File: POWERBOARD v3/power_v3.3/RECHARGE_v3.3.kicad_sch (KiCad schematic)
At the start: 27 parts, among them J1 2053380003, J2 UJ20-C-H-G-SMT-1-P16-TR, U1 USBLC6-2, U2 BQ25886RGE

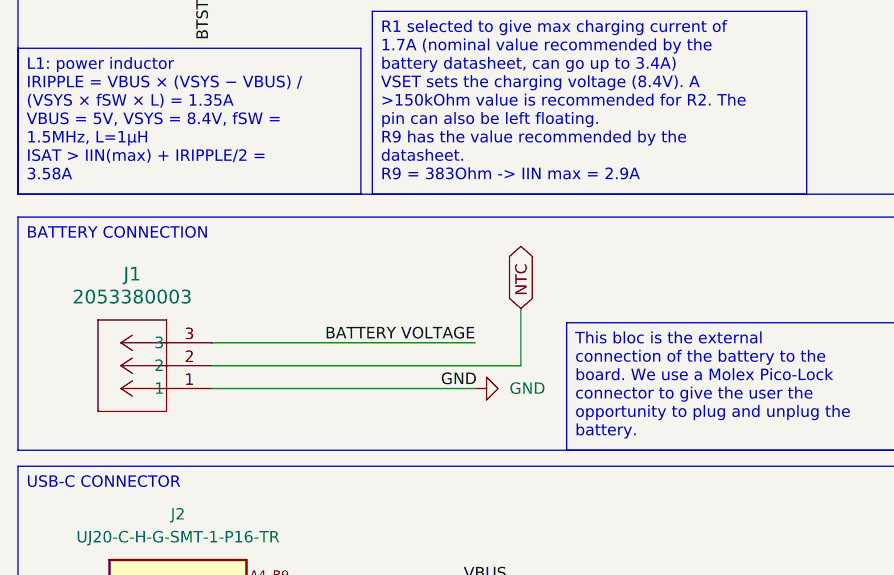
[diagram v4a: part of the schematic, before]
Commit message: changed battery connection
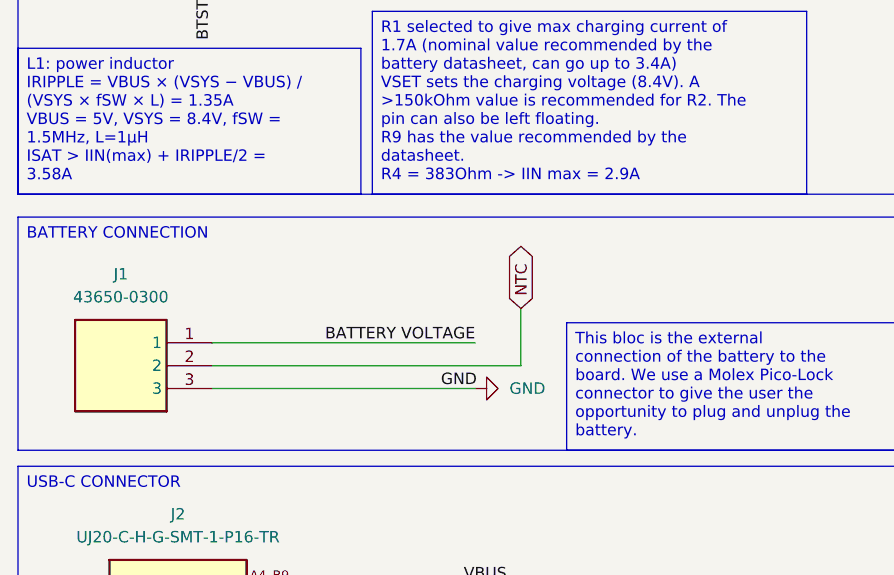
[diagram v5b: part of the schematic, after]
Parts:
- removed J1: 2053380003, footprintsusbc:CONN_2053380000-SD_03_MOL, symbol 2026-10-06_11-57-55:2053380003
- added J1: 43650-0300, 436500300, symbol 43650-0300:43650-0300
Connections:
- net BATTERY VOLTAGE: now also J1.1
- net GND: now also J1.3
- net NTC: now also J1.2
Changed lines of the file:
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@@
 		)
 	)
-	(text_box "R1 selected to give max charging current of 1.7A (nominal value recommended by the battery datasheet, can go up to 3.4A)\nVSET sets the charging voltage (8.4V). A >150kOhm value is recommended for R2. The pin can also be left floating.\nR9 has the value recommended by the datasheet.\nR9 = 383Ohm -> IIN max = 2.9A"
+	(text_box "R1 selected to give max charging current of 1.7A (nominal value recommended by the battery datasheet, can go up to 3.4A)\nVSET sets the charging voltage (8.4V). A >150kOhm value is recommended for R2. The pin can also be left floating.\nR9 has the value recommended by the datasheet.\nR4 = 383Ohm -> IIN max = 2.9A"
 		(exclude_from_sim no)
 		(at 67.31 68.58 0)
@@
 	)
 	(symbol
+		(lib_id "43650-0300:43650-0300")
+		(at 49.53 110.49 180)
+		(unit 1)
+		(body_style 1)
+		(exclude_from_sim no)
+		(in_bom yes)
+		(on_board yes)
+		(in_pos_files yes)
+		(dnp no)
+		(fields_autoplaced yes)
+		(property "Reference" "J1"
+			(at 39.37 97.79 0)
+			(show_name no)
+			(do_not_autoplace no)
+			(effects
+				(font
+					(size 1.27 1.27)
+				)
+			)
+		)
+		(property "Value" "43650-0300"
+			(at 39.37 100.33 0)
+			(show_name no)
+			(do_not_autoplace no)
+			(effects
+				(font
+					(size 1.27 1.27)
+				)
+			)
+		)
+		(property "Footprint" "436500300"
+			(at 33.02 15.57 0)
+			(hide yes)
+			(show_name no)
+			(do_not_autoplace no)
+			(effects
+				(font
+					(size 1.27 1.27)
+				)
+				(justify left top)
+			)
+		)
+		(property "Datasheet" "https://www.molex.com/pdm_docs/sd/436500200_sd.pdf"
+			(at 33.02 -84.43 0)
+			(hide yes)
+			(show_name no)
+			(do_not_autoplace no)
+			(effects
+				(font
+					(size 1.27 1.27)
+				)
+				(justify left top)
+			)
+		)
+		(property "Description" "Micro-Fit 3.0 Right-Angle Header, 3.00mm Pitch, Single Row, 3 Circuits, with Snap-in Plastic Peg PCB Lock, Glow-Wire Capable, Black"
+			(at 49.53 110.49 0)
+			(hide yes)
+			(show_name no)
+			(do_not_autoplace no)
+			(effects
+				(font
+					(size 1.27 1.27)
+				)
+			)
+		)
+		(property "Height" "13.56"
+			(at 33.02 -284.43 0)
+			(hide yes)
+			(show_name no)
+			(do_not_autoplace no)
+			(effects
+				(font
+					(size 1.27 1.27)
+				)
+				(justify left top)
+			)
+		)
+		(property "Mouser Part Number" "538-43650-0300"
+			(at 33.02 -384.43 0)
+			(hide yes)
+			(show_name no)
+			(do_not_autoplace no)
+			(effects
+				(font
+					(size 1.27 1.27)
+				)
+				(justify left top)
+			)
+		)
+		(property "Mouser Price/Stock" "https://www.mouser.co.uk/ProductDetail/Molex/43650-0300?qs=P7cO%252B%252BFDLzTpuYfoYulxAA%3D%3D"
+			(at 33.02 -484.43 0)
+			(hide yes)
+			(show_name no)
+			(do_not_autoplace no)
+			(effects
+				(font
+					(size 1.27 1.27)
+				)
+				(justify left top)
+			)
+		)
+		(property "Manufacturer_Name" "Molex"
+			(at 33.02 -584.43 0)
+			(hide yes)
+			(show_name no)
+			(do_not_autoplace no)
+			(effects
+				(font
+					(size 1.27 1.27)
+				)
+				(justify left top)
+			)
+		)
+		(property "Manufacturer_Part_Number" "43650-0300"
+			(at 33.02 -684.43 0)
+			(hide yes)
+			(show_name no)
+			(do_not_autoplace no)
+			(effects
+				(font
+					(size 1.27 1.27)
+				)
+				(justify left top)
+			)
+		)
+		(pin "1"
+		)
+		(pin "2"
+		)
+		(pin "3"
+		)
+		(instances
+			(project "power_v3.3"
+				(path "/432bcdcf-747a-4fa0-b87b-096f44260199/ef6b3a2b-31e3-4ffb-9457-e6034dbdb4b5"
+					(reference "J1")
+					(unit 1)
+				)
+			)
+		)
+	)
+	(symbol
 		(lib_id "Device:C")
 		(at 148.59 48.26 0)
@@
 					(unit 1)
 				)
-			)
-		)
-	)
-	(symbol
-		(lib_id "2026-10-06_11-57-55:2053380003")
-		(at 49.53 110.49 180)
-		(unit 1)
-		(body_style 1)
-		(exclude_from_sim no)
-		(in_bom yes)
-		(on_board yes)
-		(in_pos_files yes)
-		(dnp no)
-		(fields_autoplaced yes)
-		(property "Reference" "J1"
-			(at 40.64 97.79 0)
-			(show_name no)
-			(do_not_autoplace no)
-			(effects
-				(font
-					(size 1.524 1.524)
-				)
-			)
-		)
-		(property "Value" "2053380003"
-			(at 40.64 100.33 0)
-			(show_name no)
-			(do_not_autoplace no)
-			(effects
-				(font
-					(size 1.524 1.524)
-				)
-			)
-		)
-		(property "Footprint" "footprintsusbc:CONN_2053380000-SD_03_MOL"
-			(at 49.53 110.49 0)
-			(hide yes)
-			(show_name no)
-			(do_not_autoplace no)
-			(effects
-				(font
-					(size 1.27 1.27)
-					(italic yes)
-				)
-			)
-		)
-		(property "Datasheet" "https://www.molex.com/en-us/products/part-detail-pdf/2053380003?display=pdf"
-			(at 49.53 110.49 0)
-			(hide yes)
-			(show_name no)
-			(do_not_autoplace no)
-			(effects
-				(font
-					(size 1.27 1.27)
-					(italic yes)
-				)
-			)
-		)
-		(property "Description" ""
-			(at 49.53 110.49 0)
-			(hide yes)
-			(show_name no)
-			(do_not_autoplace no)
-			(effects
-				(font
-					(size 1.27 1.27)
-				)
-			)
-		)
-		(pin "2"
-		)
-		(pin "3"
-		)
-		(pin "1"
-		)
-		(instances
-			(project "power_v3.3"
-				(path "/432bcdcf-747a-4fa0-b87b-096f44260199/ef6b3a2b-31e3-4ffb-9457-e6034dbdb4b5"
-					(reference "J1")
-					(unit 1)
-				)
